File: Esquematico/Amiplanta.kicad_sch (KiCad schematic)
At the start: 0 parts

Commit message: intento push
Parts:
- added R?: R, symbol Device:R
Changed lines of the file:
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@@
     (stroke (width 0) (type default) (color 0 0 0 0))
+  )
+  (symbol (lib_id "Device:R") (at 212.09 53.34 0) (unit 1)
+    (in_bom yes) (on_board yes) (fields_autoplaced)
+    (property "Reference" "R?" (id 0) (at 214.63 52.0699 0)
+      (effects (font (size 1.27 1.27)) (justify left))
+    )
+    (property "Value" "R" (id 1) (at 214.63 54.6099 0)
+      (effects (font (size 1.27 1.27)) (justify left))
+    )
+    (property "Footprint" "" (id 2) (at 210.312 53.34 90)
+      (effects (font (size 1.27 1.27)) hide)
+    )
+    (property "Datasheet" "~" (id 3) (at 212.09 53.34 0)
+      (effects (font (size 1.27 1.27)) hide)
+    )
+    (pin "1")
+    (pin "2")
   )
   (sheet (at 72.39 78.74) (size 13.97 7.62) (fields_autoplaced)
@@
       (reference "R1") (unit 1) (value "R") (footprint "")
     )
+    (path "/058d58a0-1c80-40e3-b9b3-c8131e764feb"
+      (reference "R?") (unit 1) (value "R") (footprint "")
+    )
     (path "/f208f94e-d25e-4624-bb7e-be2762749fd2/bd14b65c-997b-41da-bf84-2d98b196f72f"

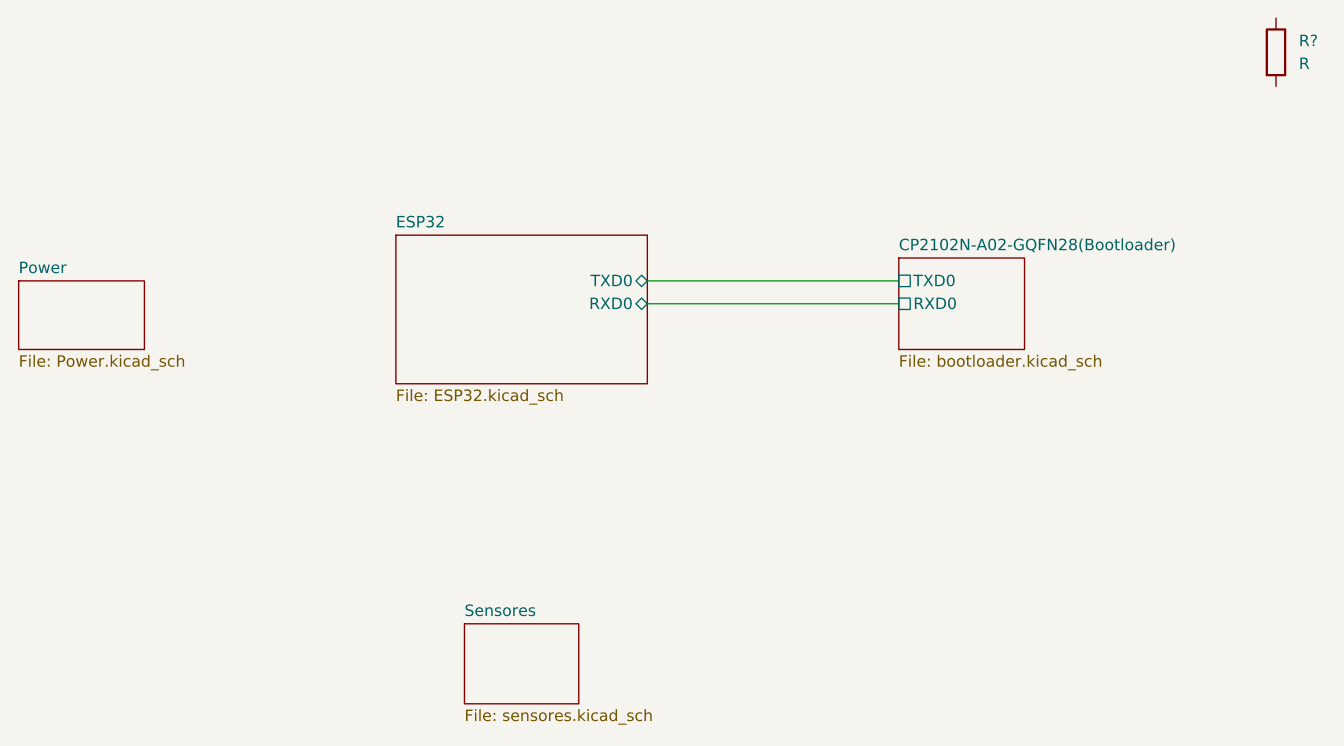
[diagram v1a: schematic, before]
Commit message: Circuito Pantalla Oled SSD1306 implementado. Modelo y Footprints SD1306 agregados
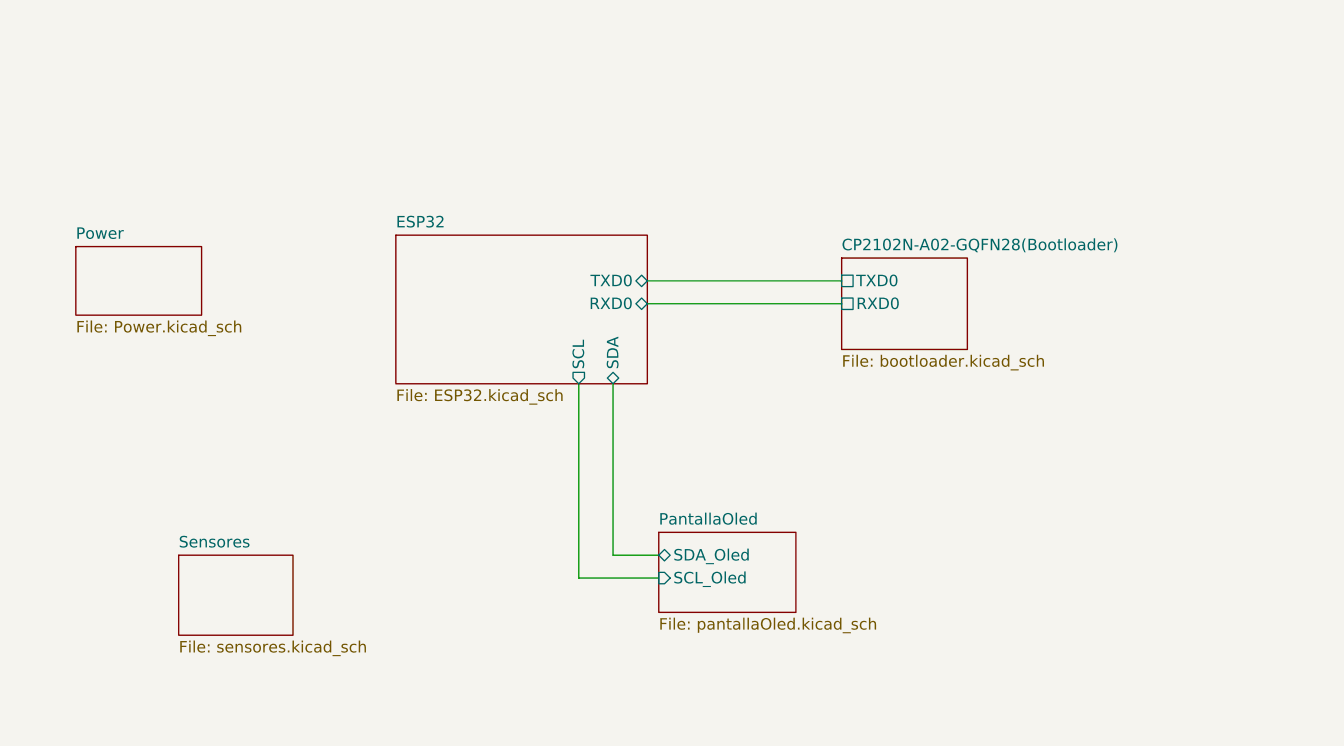
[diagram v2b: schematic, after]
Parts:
- removed R?: R, symbol Device:R
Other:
- added sheet PantallaOled (pantallaOled.kicad_sch)
- sheet ESP32 ports: added SCL, SDA; removed none
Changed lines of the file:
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@@
 (kicad_sch (version 20211123) (generator eeschema)
   (paper "A4")
-  (wire (pts (xy 142.24 81.28) (xy 170.18 81.28))
-    (stroke (width 0) (type default) (color 0 0 0 0))
-  )
-  (wire (pts (xy 142.24 78.74) (xy 170.18 78.74))
-    (stroke (width 0) (type default) (color 0 0 0 0))
-  )
-  (symbol (lib_id "Device:R") (at 212.09 53.34 0) (unit 1)
-    (in_bom yes) (on_board yes) (fields_autoplaced)
-    (property "Reference" "R?" (id 0) (at 214.63 52.0699 0)
-      (effects (font (size 1.27 1.27)) (justify left))
-    )
-    (property "Value" "R" (id 1) (at 214.63 54.6099 0)
-      (effects (font (size 1.27 1.27)) (justify left))
-    )
-    (property "Footprint" "" (id 2) (at 210.312 53.34 90)
-      (effects (font (size 1.27 1.27)) hide)
-    )
-    (property "Datasheet" "~" (id 3) (at 212.09 53.34 0)
-      (effects (font (size 1.27 1.27)) hide)
-    )
-    (pin "1")
-    (pin "2")
-  )
-  (sheet (at 72.39 78.74) (size 13.97 7.62) (fields_autoplaced)
-    (stroke (width 0.1524) (type solid) (color 0 0 0 0))
-    (fill (color 0 0 0 0.0000))
-    (property "Sheet name" "Power" (id 0) (at 72.39 78.0284 0)
-      (effects (font (size 1.27 1.27)) (justify left bottom))
-    )
-    (property "Sheet file" "Power.kicad_sch" (id 1) (at 72.39 86.9446 0)
-      (effects (font (size 1.27 1.27)) (justify left top))
-    )
-  )
-  (sheet (at 121.92 116.84) (size 12.7 8.89) (fields_autoplaced)
-    (stroke (width 0.1524) (type solid) (color 0 0 0 0))
-    (fill (color 0 0 0 0.0000))
-    (property "Sheet name" "Sensores" (id 0) (at 121.92 116.1284 0)
-      (effects (font (size 1.27 1.27)) (justify left bottom))
-    )
-    (property "Sheet file" "sensores.kicad_sch" (id 1) (at 121.92 126.3146 0)
+  (wire (pts (xy 143.51 111.76) (xy 134.62 111.76))
+    (stroke (width 0) (type default) (color 0 0 0 0))
+  )
+  (wire (pts (xy 134.62 111.76) (xy 134.62 90.17))
+    (stroke (width 0) (type default) (color 0 0 0 0))
+  )
+  (wire (pts (xy 138.43 109.22) (xy 138.43 90.17))
+    (stroke (width 0) (type default) (color 0 0 0 0))
+  )
+  (wire (pts (xy 142.24 81.28) (xy 163.83 81.28))
+    (stroke (width 0) (type default) (color 0 0 0 0))
+  )
+  (wire (pts (xy 142.24 78.74) (xy 163.83 78.74))
+    (stroke (width 0) (type default) (color 0 0 0 0))
+  )
+  (wire (pts (xy 143.51 109.22) (xy 138.43 109.22))
+    (stroke (width 0) (type default) (color 0 0 0 0))
+  )
+  (sheet (at 143.51 106.68) (size 15.24 8.89) (fields_autoplaced)
+    (stroke (width 0.1524) (type solid) (color 50 226 255 1))
+    (fill (color 252 238 255 1.0000))
+    (property "Sheet name" "PantallaOled" (id 0) (at 143.51 105.9684 0)
+      (effects (font (size 1.27 1.27)) (justify left bottom))
+    )
+    (property "Sheet file" "pantallaOled.kicad_sch" (id 1) (at 143.51 116.1546 0)
+      (effects (font (size 1.27 1.27)) (justify left top))
+    )
+    (pin "SCL_Oled" input (at 143.51 111.76 180)
+      (effects (font (size 1.27 1.27)) (justify left))
+    )
+    (pin "SDA_Oled" bidirectional (at 143.51 109.22 180)
+      (effects (font (size 1.27 1.27)) (justify left))
+    )
+  )
+  (sheet (at 78.74 74.93) (size 13.97 7.62) (fields_autoplaced)
+    (stroke (width 0.1524) (type solid) (color 0 0 0 0))
+    (fill (color 0 0 0 0.0000))
+    (property "Sheet name" "Power" (id 0) (at 78.74 74.2184 0)
+      (effects (font (size 1.27 1.27)) (justify left bottom))
+    )
+    (property "Sheet file" "Power.kicad_sch" (id 1) (at 78.74 83.1346 0)
+      (effects (font (size 1.27 1.27)) (justify left top))
+    )
+  )
+  (sheet (at 90.17 109.22) (size 12.7 8.89) (fields_autoplaced)
+    (stroke (width 0.1524) (type solid) (color 0 0 0 0))
+    (fill (color 0 0 0 0.0000))
+    (property "Sheet name" "Sensores" (id 0) (at 90.17 108.5084 0)
+      (effects (font (size 1.27 1.27)) (justify left bottom))
+    )
+    (property "Sheet file" "sensores.kicad_sch" (id 1) (at 90.17 118.6946 0)
       (effects (font (size 1.27 1.27)) (justify left top))
     )
@@
       (effects (font (size 1.27 1.27)) (justify right))
     )
-  )
-  (sheet (at 170.18 76.2) (size 13.97 10.16) (fields_autoplaced)
-    (stroke (width 0.1524) (type solid) (color 0 0 0 0))
-    (fill (color 0 0 0 0.0000))
-    (property "Sheet name" "CP2102N-A02-GQFN28(Bootloader)" (id 0) (at 170.18 75.4884 0)
-      (effects (font (size 1.27 1.27)) (justify left bottom))
-    )
-    (property "Sheet file" "bootloader.kicad_sch" (id 1) (at 170.18 86.9446 0)
-      (effects (font (size 1.27 1.27)) (justify left top))
-    )
-    (pin "TXD0" passive (at 170.18 78.74 180)
-      (effects (font (size 1.27 1.27)) (justify left))
-    )
-    (pin "RXD0" passive (at 170.18 81.28 180)
+    (pin "SDA" bidirectional (at 138.43 90.17 270)
+      (effects (font (size 1.27 1.27)) (justify left))
+    )
+    (pin "SCL" output (at 134.62 90.17 270)
+      (effects (font (size 1.27 1.27)) (justify left))
+    )
+  )
+  (sheet (at 163.83 76.2) (size 13.97 10.16) (fields_autoplaced)
+    (stroke (width 0.1524) (type solid) (color 0 0 0 0))
+    (fill (color 0 0 0 0.0000))
+    (property "Sheet name" "CP2102N-A02-GQFN28(Bootloader)" (id 0) (at 163.83 75.4884 0)
+      (effects (font (size 1.27 1.27)) (justify left bottom))
+    )
+    (property "Sheet file" "bootloader.kicad_sch" (id 1) (at 163.83 86.9446 0)
+      (effects (font (size 1.27 1.27)) (justify left top))
+    )
+    (pin "TXD0" passive (at 163.83 78.74 180)
+      (effects (font (size 1.27 1.27)) (justify left))
+    )
+    (pin "RXD0" passive (at 163.83 81.28 180)
       (effects (font (size 1.27 1.27)) (justify left))
     )
@@
     (path "/e140a476-2c20-4832-a6c9-c446e5aea50a" (page "4"))
     (path "/f208f94e-d25e-4624-bb7e-be2762749fd2" (page "5"))
+    (path "/8e21bd33-9ddd-4dab-ba12-f74e7908b709" (page "6"))
   )
   (symbol_instances
@@
       (reference "#PWR?") (unit 1) (value "GNDREF") (footprint "")
     )
+    (path "/8e21bd33-9ddd-4dab-ba12-f74e7908b709/87803d0e-08cf-4ed7-98f1-f45b59255ebc"
+      (reference "#PWR?") (unit 1) (value "GNDREF") (footprint "")
+    )
     (path "/f208f94e-d25e-4624-bb7e-be2762749fd2/aa6066d2-09de-4e1a-8588-4799a8766a9a"
       (reference "#PWR?") (unit 1) (value "GNDREF") (footprint "")
@@
       (reference "#PWR?") (unit 1) (value "GNDREF") (footprint "")
     )
+    (path "/8e21bd33-9ddd-4dab-ba12-f74e7908b709/e6d68318-68f4-4288-ba37-a6d71601cf22"
+      (reference "#PWR?") (unit 1) (value "+5V") (footprint "")
+    )
+    (path "/8e21bd33-9ddd-4dab-ba12-f74e7908b709/e47284f7-90b7-4661-a5d8-4f12b1a5faed"
+      (reference "Brd?") (unit 1) (value "SSD1306") (footprint "SSD1306:128x64OLED")
+    )
     (path "/9a453819-a545-42f7-8ffc-01e63c178689/2c744707-48df-4d4b-b32c-f02a8e8a95ba"
       (reference "C1") (unit 1) (value "1u") (footprint "")
@@
       (reference "R1") (unit 1) (value "R") (footprint "")
     )
-    (path "/058d58a0-1c80-40e3-b9b3-c8131e764feb"
-      (reference "R?") (unit 1) (value "R") (footprint "")
-    )
     (path "/f208f94e-d25e-4624-bb7e-be2762749fd2/bd14b65c-997b-41da-bf84-2d98b196f72f"

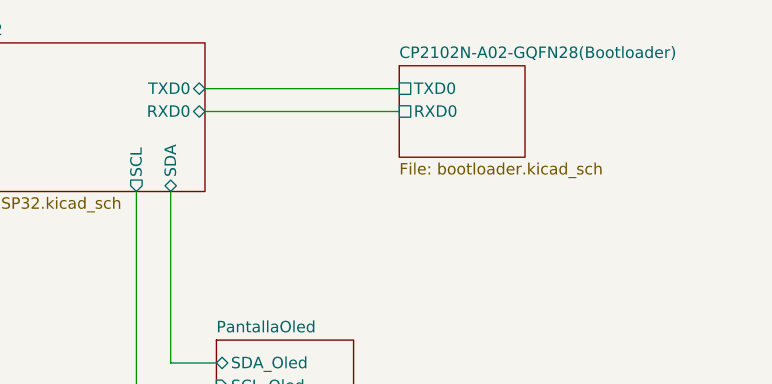
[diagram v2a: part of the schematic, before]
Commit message: Agregado circuito de potencia a través de Jack y selector de posición para alimentar de USB, Jack o apagar
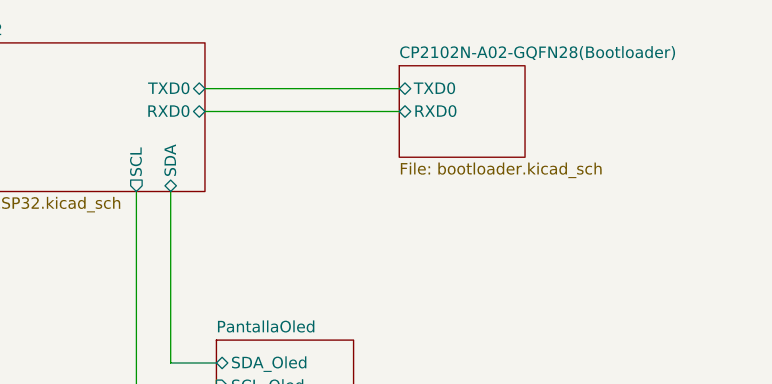
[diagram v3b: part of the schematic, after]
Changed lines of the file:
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@@
       (effects (font (size 1.27 1.27)) (justify left top))
     )
-    (pin "TXD0" passive (at 163.83 78.74 180)
+    (pin "TXD0" bidirectional (at 163.83 78.74 180)
       (effects (font (size 1.27 1.27)) (justify left))
     )
-    (pin "RXD0" passive (at 163.83 81.28 180)
+    (pin "RXD0" bidirectional (at 163.83 81.28 180)
       (effects (font (size 1.27 1.27)) (justify left))
     )
@@
       (reference "#PWR0115") (unit 1) (value "GNDREF") (footprint "")
     )
+    (path "/9a453819-a545-42f7-8ffc-01e63c178689/06bc27f0-8f67-4b42-a02d-402ce0b10715"
+      (reference "#PWR?") (unit 1) (value "GNDREF") (footprint "")
+    )
     (path "/e140a476-2c20-4832-a6c9-c446e5aea50a/1a0ea9e8-2171-41c9-be11-894122e30cbe"
       (reference "#PWR?") (unit 1) (value "GNDREF") (footprint "")
@@
       (reference "#PWR?") (unit 1) (value "GNDREF") (footprint "")
     )
+    (path "/9a453819-a545-42f7-8ffc-01e63c178689/6ed08958-febf-40cd-b13e-7b76a14cdf5b"
+      (reference "#PWR?") (unit 1) (value "+5V") (footprint "")
+    )
     (path "/f208f94e-d25e-4624-bb7e-be2762749fd2/754ff81b-77e5-4b67-83fa-84517bf546a2"
       (reference "#PWR?") (unit 1) (value "GNDREF") (footprint "")
@@
       (reference "#PWR?") (unit 1) (value "GNDREF") (footprint "")
     )
+    (path "/9a453819-a545-42f7-8ffc-01e63c178689/91c331a8-f30d-4604-a3aa-c1e292ae95bf"
+      (reference "#PWR?") (unit 1) (value "GNDREF") (footprint "")
+    )
     (path "/f208f94e-d25e-4624-bb7e-be2762749fd2/aa6066d2-09de-4e1a-8588-4799a8766a9a"
       (reference "#PWR?") (unit 1) (value "GNDREF") (footprint "")
-    )
-    (path "/f208f94e-d25e-4624-bb7e-be2762749fd2/ae0fc72f-4f9f-45f4-a568-fb95e199f172"
-      (reference "#PWR?") (unit 1) (value "+5V") (footprint "")
     )
     (path "/f208f94e-d25e-4624-bb7e-be2762749fd2/b04ffc44-8fce-4a2a-8ec1-8e26701fc860"
@@
       (reference "Cfeed2") (unit 1) (value "0.1uF/50(10%)") (footprint "Capacitor_SMD:C_1210_3225Metric_Pad1.33x2.70mm_HandSolder")
     )
+    (path "/9a453819-a545-42f7-8ffc-01e63c178689/2d6eb9c3-c12a-4db4-b9f5-ec34a44d226a"
+      (reference "D?") (unit 1) (value "MBR1020VL") (footprint "Diode_SMD:D_SOD-123F")
+    )
+    (path "/9a453819-a545-42f7-8ffc-01e63c178689/775bc2ee-a439-4a93-a5a2-0dcd9f65d5c6"
+      (reference "DJackPwr") (unit 1) (value "LESD5D5.0CT1G") (footprint "TVS_LESD5D5.0CT1G")
+    )
     (path "/f208f94e-d25e-4624-bb7e-be2762749fd2/e3814a41-99f9-434a-98ee-7bf303d19ca2"
       (reference "DUSBBAT") (unit 1) (value "BAT760-7") (footprint "SOD2513X120N")
@@
       (reference "J?") (unit 1) (value "USB_B_Micro") (footprint "")
     )
+    (path "/9a453819-a545-42f7-8ffc-01e63c178689/a21fd23b-10fd-4ea0-984d-cf4be95b7984"
+      (reference "J?") (unit 1) (value "Jack-DC") (footprint "")
+    )
     (path "/f208f94e-d25e-4624-bb7e-be2762749fd2/27f6d6bc-db2e-4dcc-866c-e499eea67225"
       (reference "Q?") (unit 1) (value "SS8050-G") (footprint "TRANS_SS8050-G")
@@
       (reference "Rvbus2") (unit 1) (value "47.5K(5%)") (footprint "")
     )
+    (path "/9a453819-a545-42f7-8ffc-01e63c178689/2af25db5-ea0f-4b1e-89f7-0f2918b5fa2b"
+      (reference "SW?") (unit 1) (value "SW_DP3T") (footprint "")
+    )
     (path "/e140a476-2c20-4832-a6c9-c446e5aea50a/501ef5bb-8a5b-4bc2-8a13-cbd172362c89"
